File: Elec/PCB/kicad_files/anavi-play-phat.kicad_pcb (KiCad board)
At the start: 2 copper layers, 77.6 x 30 mm, 13 parts, among them J2 USB_A_PLUG

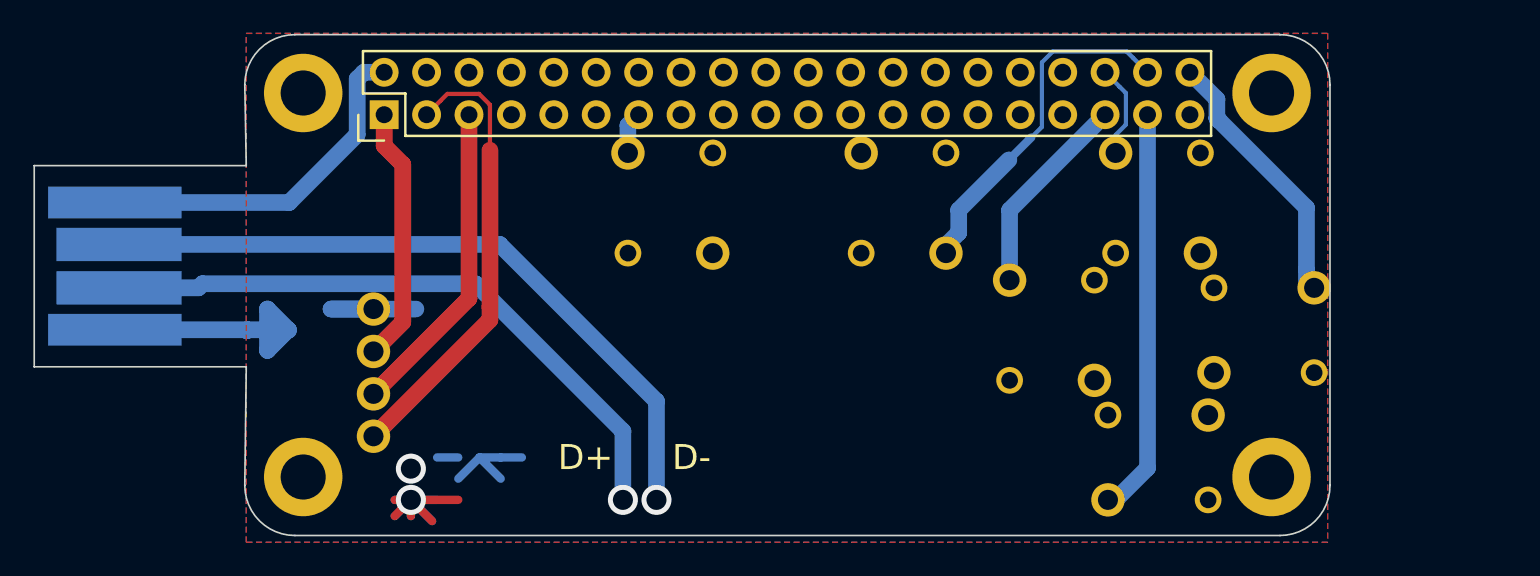
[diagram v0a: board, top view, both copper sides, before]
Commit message: PCB v3 correction USB
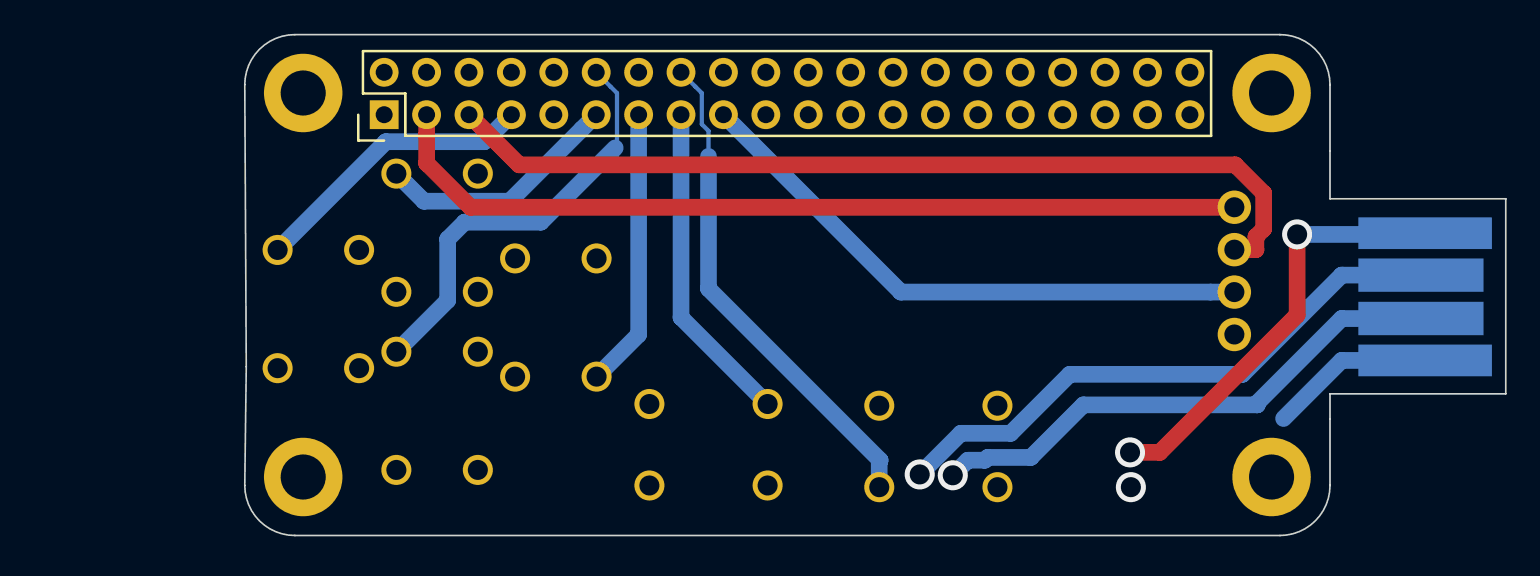
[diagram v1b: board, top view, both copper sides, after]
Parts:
- removed SW_BCK1, SW_DNW1, SW_L1, SW_OK1, SW_R1, SW_UP1: boutton_5mx6m, boutton:boutton__5mx5m
- added BCK1: boutton_6mx6m, boutton:boutton__6mx6m, B.Cu at (190.0, 99.7)
- added DWN1: boutton_6mx6m, boutton:boutton__6mx6m, B.Cu at (160.0, 97.5)
- added L1: boutton_6mx6m, boutton:boutton__6mx6m, B.Cu at (167.1, 91.9)
- added OK1: boutton_6mx6m, boutton:boutton__6mx6m, B.Cu at (176.3, 99.6)
- added R1: boutton_6mx6m, boutton:boutton__6mx6m, B.Cu at (152.9, 91.4)
- added UP1: boutton_6mx6m, boutton:boutton__6mx6m, B.Cu at (160.0, 86.9)
- moved J2 88.3 mm to (224.1, 90.7), turned to 270 degrees
- moved i2c_scr1 51.6 mm to (207.8, 93.0), turned to 180 degrees
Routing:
- net Net-(RASP_CONN1-Pad5): track 19.1 -> 54.7 mm
- net Net-(BCK1-Pad2): track 0.00 -> 29.8 mm
- net Net-(DWN1-Pad2): track 0.10 -> 25.5 mm
- net Net-(RASP_CONN1-Pad3): track 27.9 -> 53.0 mm
- net Net-(RASP_CONN1-Pad37): track 24.3 -> 0.43 mm
- net +5V: track 21.8 -> 0.46 mm, vias 1 -> 0
- net Net-(RASP_CONN1-Pad38): track 20.5 -> 0.00 mm
- net GND: track 29.6 -> 9.92 mm
- net +3V3: track 15.8 -> 35.5 mm
- net Net-(OK1-Pad2): track 0.00 -> 19.5 mm
- net Net-(R1-Pad2): track 0.00 -> 17.4 mm
- net Net-(RASP_CONN1-Pad40): track 16.0 -> 0.00 mm
- net Net-(RASP_CONN1-Pad11): track 0.04 -> 14.8 mm
- net Net-(L1-Pad2): track 3.02 -> 16.7 mm
- net Net-(RASP_CONN1-Pad35): track 12.7 -> 0.00 mm
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- removed copper zone on B.Cu, net GND
- removed copper zone on F.Cu, net GND
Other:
- board size 77.6 x 30 mm -> 75.5 x 30 mm
- board text removed: "D+"
- board text removed: "D-"

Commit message: pcb mieux
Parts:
- added ?: , , F.Cu at (227.1, 91.5)
- added ?: , , F.Cu at (219.3, 90.7)
- added REF**: KEYBOX, myfootprint:KEYBOX, B.Cu at (219.2, 90.5)
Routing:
- net GND: track 9.92 -> 0.00 mm
- net (no net): track 92.9 -> 102.8 mm

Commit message: j'avais pas save déso
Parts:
- removed REF**: KEYBOX, myfootprint:KEYBOX

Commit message: export du pcb version 2.5
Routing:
- net GND: track 0.00 -> 6.01 mm
- added copper zone on B.Cu, net GND
- added copper zone on F.Cu, net GND
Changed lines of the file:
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@@
     (thickness 1.6)
     (drawings 19)
-    (tracks 94)
+    (tracks 103)
     (zones 0)
     (modules 15)
@@
   )
   (setup
-    (last_trace_width 1)
+    (last_trace_width 0.5)
     (user_trace_width 0.254)
     (user_trace_width 0.5)
@@
     (pad_to_mask_clearance 0)
     (aux_axis_origin 0 0)
-    (visible_elements FFFFFF7F)
+    (visible_elements FFFFF77F)
     (pcbplotparams
       (layerselection 0x01000_ffffffff)
@@
   (gr_arc (start 151.5011 102.0036) (end 148.5011 102.0036) (angle -90) (layer Edge.Cuts) (width 0.1))
   (gr_circle (center 152.0011 101.5036) (end 152.0011 101.5036) (layer Edge.Cuts) (width 0.1))
-  (via (at 201.5744 102.108) (size 1.8) (drill 1.2) (layers F.Cu B.Cu) (net 2))
   (via (at 201.5236 100.0252) (size 1.8) (drill 1.2) (layers F.Cu B.Cu) (net 0))
   (via (at 190.9064 101.3968) (size 1.8) (drill 1.2) (layers F.Cu B.Cu) (net 0))
@@
   (segment (start 219.1264 86.9696) (end 219.198 86.898) (width 1) (layer B.Cu) (net 0))
   (segment (start 211.5312 86.9696) (end 219.1264 86.9696) (width 1) (layer B.Cu) (net 0))
+  (segment (start 219.198 94.518) (end 214.198 94.518) (width 1) (layer B.Cu) (net 0))
+  (segment (start 213.4824 94.518) (end 214.198 94.518) (width 0.5) (layer B.Cu) (net 0))
+  (segment (start 213.0044 94.996) (end 213.4824 94.518) (width 0.5) (layer B.Cu) (net 0))
+  (segment (start 213.3092 95.3516) (end 213.3644 95.3516) (width 0.5) (layer B.Cu) (net 0))
+  (segment (start 213.1568 95.25) (end 213.6648 94.742) (width 0.5) (layer B.Cu) (net 0))
+  (segment (start 212.9536 95.25) (end 213.1568 95.25) (width 0.5) (layer B.Cu) (net 0))
+  (segment (start 213.3644 95.3516) (end 213.6648 94.742) (width 0.5) (layer B.Cu) (net 0))
+  (segment (start 213.6648 94.742) (end 214.198 94.518) (width 0.5) (layer B.Cu) (net 0))
+  (segment (start 213.3644 95.3516) (end 214.198 94.518) (width 0.5) (layer B.Cu) (net 0))
   (segment (start 177.165 79.756) (end 177.17 79.8) (width 0.5) (layer F.Cu) (net 1) (status 80000))
   (segment (start 156.845 80.137) (end 156.845 79.756) (width 0.5) (layer B.Cu) (net 1) (status 80000))
@@
   (segment (start 187.794 90.424) (end 206.357787 90.424) (width 1) (layer B.Cu) (net 1))
   (segment (start 177.17 79.8) (end 187.794 90.424) (width 1) (layer B.Cu) (net 1))
-  (segment (start 214.198 94.518) (end 210.7184 97.9976) (width 1) (layer B.Cu) (net 0))
-  (segment (start 219.198 94.518) (end 214.198 94.518) (width 1) (layer B.Cu) (net 0))
+  (via (at 201.5744 102.108) (size 1.8) (drill 1.2) (layers F.Cu B.Cu) (net 2))
+  (segment (start 163.482 83.328) (end 162.46 83.328) (width 1) (layer B.Cu) (net 2))
+  (segment (start 167.01 79.8) (end 163.482 83.328) (width 1) (layer B.Cu) (net 2))
   (segment (start 156.85 77.26) (end 156.845 77.216) (width 0.5) (layer F.Cu) (net 3) (status 80000))
   (segment (start 156.85 77.26) (end 156.547 77.26) (width 0.5) (layer B.Cu) (net 3))
@@
   (segment (start 167.01 77.26) (end 167.01 77.5285) (width 0.254) (layer F.Cu) (net 10))
   (segment (start 167.01 77.26) (end 167.31 77.26) (width 0.254) (layer F.Cu) (net 10))
-  (segment (start 169.55 77.26) (end 169.545 77.216) (width 0.5) (layer B.Cu) (net 28) (status 80000))
-  (segment (start 169.55 77.26) (end 169.5 77.25) (width 0.5) (layer B.Cu) (net 28) (status 80000))
   (segment (start 189.87 79.8) (end 189.909 79.8) (width 0.5) (layer F.Cu) (net 18))
   (segment (start 189.865 80.137) (end 189.865 79.756) (width 0.5) (layer F.Cu) (net 18) (status 80000))
@@
   (segment (start 176.276 82.296) (end 176.276 90.2208) (width 1) (layer B.Cu) (net 27))
   (segment (start 176.276 90.2208) (end 186.5536 100.4984) (width 1) (layer B.Cu) (net 27))
+  (segment (start 169.55 77.26) (end 169.545 77.216) (width 0.5) (layer B.Cu) (net 28) (status 80000))
+  (segment (start 169.55 77.26) (end 169.5 77.25) (width 0.5) (layer B.Cu) (net 28) (status 80000))
   (segment (start 157.58 93.996) (end 160.651989 90.924011) (width 1) (layer B.Cu) (net 28))
   (segment (start 161.667989 86.236011) (end 166.239989 86.236011) (width 1) (layer B.Cu) (net 28))
@@
   (segment (start 150.468 87.9) (end 156.950399 81.417601) (width 1) (layer B.Cu) (net 31))
   (segment (start 156.950399 81.417601) (end 162.852399 81.417601) (width 1) (layer B.Cu) (net 31))
+  (zone (net 0) (net_name "") (layers F&B.Cu) (hatch edge 0.508)
+    (connect_pads (clearance 0.508))
+    (min_thickness 0.254)
+    (keepout (tracks not_allowed) (vias not_allowed) (copperpour not_allowed))
+    (fill (arc_segments 32) (thermal_gap 0.508) (thermal_bridge_width 0.508))
+    (polygon
+      (pts
+        (xy 224.0788 96.52) (xy 213.4616 96.4692) (xy 213.5124 84.9376) (xy 213.537861 84.886678) (xy 224.0788 84.836)
+      )
+    )
+    (polygon
+      (pts
+        (xy 213.537861 84.886678) (xy 213.5124 84.8868) (xy 213.5632 84.836)
+      )
+    )
+  )
+  (zone (net 2) (net_name GND) (layer F.Cu) (hatch edge 0.508)
+    (connect_pads (clearance 0.508))
+    (min_thickness 0.254)
+    (fill yes (arc_segments 32) (thermal_gap 0.508) (thermal_bridge_width 0.508))
+    (polygon
+      (pts
+        (xy 213.8172 73.8632) (xy 213.5632 105.7148) (xy 148.082 105.664) (xy 147.9296 73.7108)
+      )
+    )
+  )
+  (zone (net 2) (net_name GND) (layer B.Cu) (hatch edge 0.508)
+    (connect_pads (clearance 0.508))
+    (min_thickness 0.254)
+    (fill yes (arc_segments 32) (thermal_gap 0.508) (thermal_bridge_width 0.508))
+    (polygon
+      (pts
+        (xy 213.8172 73.8632) (xy 213.5632 105.7148) (xy 148.082 105.7656) (xy 147.8788 73.8124)
+      )
+    )
+  )
 )

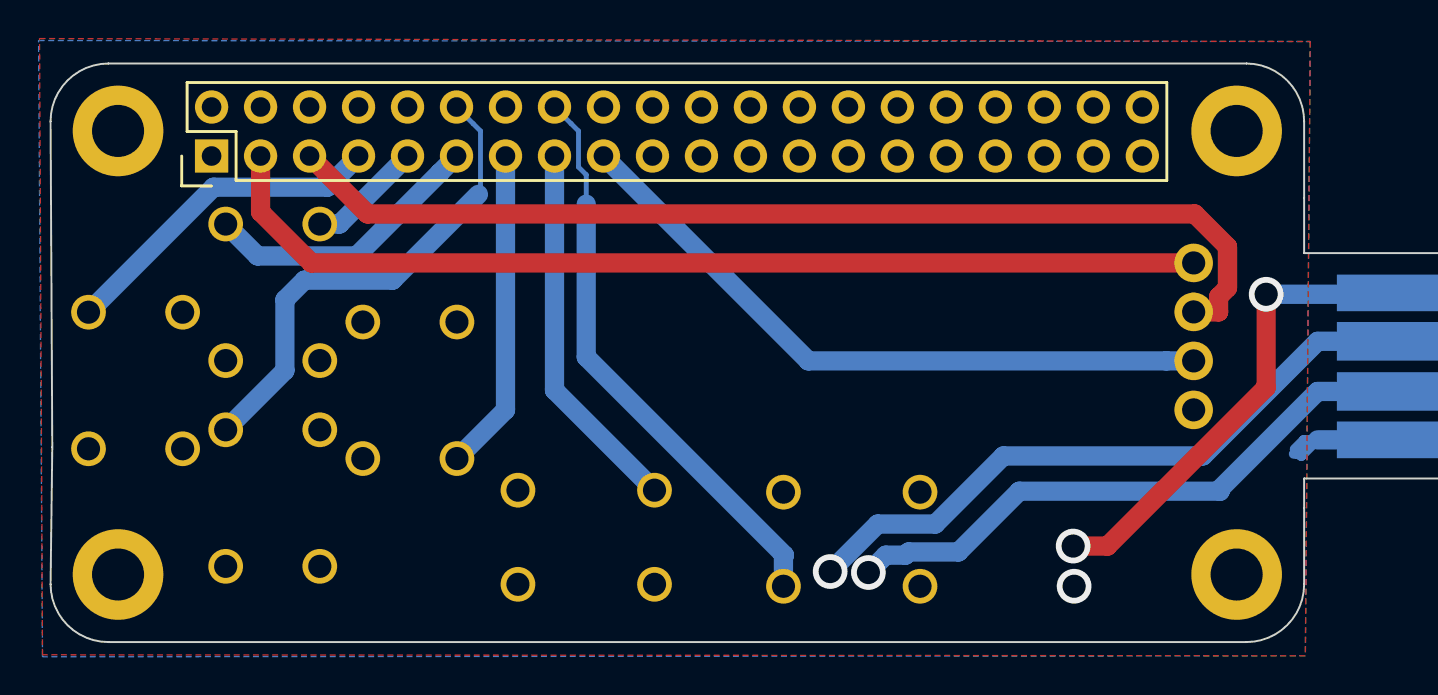
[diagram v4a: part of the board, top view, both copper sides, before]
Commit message: le pcb corrigé pour une vrai prod
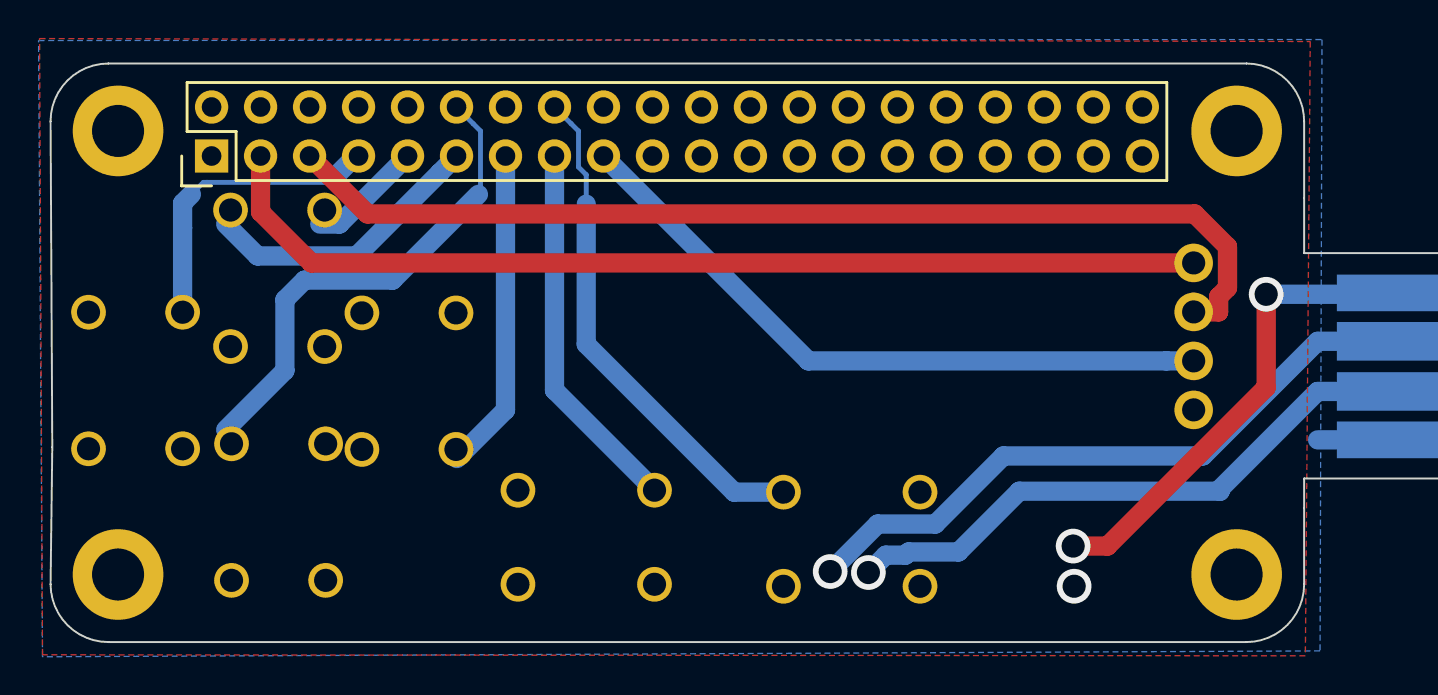
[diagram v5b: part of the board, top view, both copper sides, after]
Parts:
- moved DWN1 0.79 mm to (160.3, 98.3)
- moved UP1 0.77 mm to (160.3, 86.1)
- moved L1 0.48 mm to (167.1, 91.5)
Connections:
- J2 pad 1: (no net) -> GND
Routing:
- net (no net): track 102.7 -> 92.9 mm
- net GND: track 6.01 -> 11.0 mm
- net Net-(BCK1-Pad2): track 29.8 -> 26.4 mm
- net Net-(R1-Pad2): track 17.4 -> 15.9 mm

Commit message: Le joli pcb
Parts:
- removed ? (x2): , 
- added BCK1: boutton_6mx6m, boutton:boutton__6mx6m, B.Cu at (190.4, 163.6)
- added BCK1: boutton_6mx6m, boutton:boutton__6mx6m, B.Cu at (190.2, 131.7)
- added DWN1: boutton_6mx6m, boutton:boutton__6mx6m, B.Cu at (160.6, 162.2)
- added DWN1: boutton_6mx6m, boutton:boutton__6mx6m, B.Cu at (160.4, 130.3)
- added J1: d+ d-, w_conn_misc:header 2m spaced, F.Cu at (190.3, 166.4)
- added J1: d+ d-, w_conn_misc:header 2m spaced, F.Cu at (190.1, 134.5)
- added J1: d+ d-, w_conn_misc:header 2m spaced, F.Cu at (189.9, 102.5)
- added J2: 5v gnd, w_conn_misc:header 2m spaced, F.Cu at (202.3, 164.9)
- added J2: USB_A_PLUG, Wickerlib:CONN-USB-A-PCB-TRACES, B.Cu at (228.3, 154.8)
- added J2: 5v gnd, w_conn_misc:header 2m spaced, F.Cu at (202.1, 132.9)
- added J2: USB_A_PLUG, Wickerlib:CONN-USB-A-PCB-TRACES, B.Cu at (228.1, 122.8)
- added J2: 5v gnd, w_conn_misc:header 2m spaced, F.Cu at (201.9, 100.9)
- added L1: boutton_6mx6m, boutton:boutton__6mx6m, B.Cu at (167.4, 155.4)
- added L1: boutton_6mx6m, boutton:boutton__6mx6m, B.Cu at (167.2, 123.4)
- added OK1: boutton_6mx6m, boutton:boutton__6mx6m, B.Cu at (176.7, 163.6)
- added OK1: boutton_6mx6m, boutton:boutton__6mx6m, B.Cu at (176.5, 131.7)
- added R1: boutton_6mx6m, boutton:boutton__6mx6m, B.Cu at (153.3, 155.4)
- added R1: boutton_6mx6m, boutton:boutton__6mx6m, B.Cu at (153.1, 123.4)
- added RASP_CONN1: Raspberry_PI, Pin_Headers:Pin_Header_Straight_2x20, F.Cu at (157.3, 143.8)
- added RASP_CONN1: Raspberry_PI, Pin_Headers:Pin_Header_Straight_2x20, F.Cu at (157.1, 111.8)
- added REF1: MountingHole_2.7mm_M2.5_DIN965_Pad, Mounting_Holes:MountingHole_2.7mm_M2.5_DIN965_Pad, F.Cu at (152.4, 142.5)
- added REF1: MountingHole_2.7mm_M2.5_DIN965_Pad, Mounting_Holes:MountingHole_2.7mm_M2.5_DIN965_Pad, F.Cu at (152.2, 110.5)
- added REF2: MountingHole_2.7mm_M2.5_DIN965_Pad, Mounting_Holes:MountingHole_2.7mm_M2.5_DIN965_Pad, F.Cu at (210.4, 142.5)
- added REF2: MountingHole_2.7mm_M2.5_DIN965_Pad, Mounting_Holes:MountingHole_2.7mm_M2.5_DIN965_Pad, F.Cu at (210.2, 110.5)
- added REF3: MountingHole_2.7mm_M2.5_DIN965_Pad, Mounting_Holes:MountingHole_2.7mm_M2.5_DIN965_Pad, F.Cu at (210.4, 165.5)
- added REF3: MountingHole_2.7mm_M2.5_DIN965_Pad, Mounting_Holes:MountingHole_2.7mm_M2.5_DIN965_Pad, F.Cu at (210.2, 133.5)
- added REF4: MountingHole_2.7mm_M2.5_DIN965_Pad, Mounting_Holes:MountingHole_2.7mm_M2.5_DIN965_Pad, F.Cu at (152.4, 165.5)
- added REF4: MountingHole_2.7mm_M2.5_DIN965_Pad, Mounting_Holes:MountingHole_2.7mm_M2.5_DIN965_Pad, F.Cu at (152.2, 133.5)
- added UP1: boutton_6mx6m, boutton:boutton__6mx6m, B.Cu at (160.6, 148.6)
- added UP1: boutton_6mx6m, boutton:boutton__6mx6m, B.Cu at (160.4, 116.6)
- added i2c_scr1: i2c_screen, i2c_screen:i2c_screen, B.Cu at (208.2, 156.9)
- added i2c_scr1: i2c_screen, i2c_screen:i2c_screen, B.Cu at (208.0, 125.0)
- moved J2 3.81 mm to (227.9, 90.8)
- moved UP1 1.54 mm to (160.2, 84.6), turned to 90 degrees
- moved DWN1 0.12 mm to (160.2, 98.3), turned to 270 degrees
- moved OK1 0.09 mm to (176.3, 99.7)
- moved L1 0.09 mm to (167.0, 91.4)
- turned R1 to 180 degrees
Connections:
- J2 pad 4: (no net) -> +5V
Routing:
- net (no net): track 92.9 -> 708.6 mm, vias 4 -> 2
- net Net-(J1-Pad1): track 0.00 -> 36.2 mm
- net Net-(J1-Pad2): track 0.00 -> 33.1 mm
- net +5V: track 0.46 -> 26.0 mm, vias 0 -> 1
- net Net-(L1-Pad2): track 16.7 -> 9.20 mm
- net Net-(RASP_CONN1-Pad11): track 14.8 -> 8.05 mm
- net GND: track 11.0 -> 5.00 mm, vias 1 -> 0
- net Net-(DWN1-Pad2): track 25.5 -> 27.4 mm
- net Net-(R1-Pad2): track 15.9 -> 17.5 mm
- added copper zone on B.Cu, net (none)
- added copper zone on F.Cu, net (none)
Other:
- board size 75.5 x 30 mm -> 79.9 x 94 mm

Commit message: pcb et readme
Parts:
- removed the BCK1 at (190.4, 163.6)
- removed the BCK1 at (190.2, 131.7)
- removed the DWN1 at (160.6, 162.2)
- removed the DWN1 at (160.4, 130.3)
- removed the J1 at (190.3, 166.4)
- removed the J1 at (190.1, 134.5)
- removed the J2 at (202.3, 164.9)
- removed the J2 at (228.3, 154.8)
- removed the J2 at (202.1, 132.9)
- removed the J2 at (228.1, 122.8)
- removed the L1 at (167.4, 155.4)
- removed the L1 at (167.2, 123.4)
- removed the OK1 at (176.7, 163.6)
- removed the OK1 at (176.5, 131.7)
- removed the R1 at (153.3, 155.4)
- removed the R1 at (153.1, 123.4)
- removed the RASP_CONN1 at (157.3, 143.8)
- removed the RASP_CONN1 at (157.1, 111.8)
- removed the REF1 at (152.4, 142.5)
- removed the REF1 at (152.2, 110.5)
- removed the REF2 at (210.4, 142.5)
- removed the REF2 at (210.2, 110.5)
- removed the REF3 at (210.4, 165.5)
- removed the REF3 at (210.2, 133.5)
- removed the REF4 at (152.4, 165.5)
- removed the REF4 at (152.2, 133.5)
- removed the UP1 at (160.6, 148.6)
- removed the UP1 at (160.4, 116.6)
- removed the i2c_scr1 at (208.2, 156.9)
- removed the i2c_scr1 at (208.0, 125.0)
- moved J2 0.31 mm to (227.6, 90.8)
- moved BCK1 0.31 mm to (189.7, 99.6)
- moved DWN1 0.31 mm to (159.9, 98.2)
- moved J1 0.31 mm to (189.6, 102.4)
- moved J2 0.31 mm to (201.6, 100.9)
- moved L1 0.31 mm to (166.7, 91.4)
- moved OK1 0.31 mm to (176.0, 99.6)
- moved R1 0.31 mm to (152.6, 91.4)
- moved RASP_CONN1 0.31 mm to (156.5, 79.7)
- moved REF1 0.31 mm to (151.7, 78.4)
- moved REF2 0.31 mm to (209.7, 78.4)
- moved REF3 0.31 mm to (209.7, 101.4)
- moved REF4 0.31 mm to (151.7, 101.4)
- moved UP1 0.31 mm to (159.9, 84.5)
- moved i2c_scr1 0.31 mm to (207.5, 92.9)
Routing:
- net (no net): track 708.6 -> 0.00 mm, vias 2 -> 0
- net Net-(RASP_CONN1-Pad5): track 54.7 -> 57.9 mm
- net GND: track 5.00 -> 7.86 mm
- removed copper zone on B.Cu, net (none)
- removed copper zone on F.Cu, net (none)
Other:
- board size 79.9 x 94 mm -> 79.5 x 30 mm
